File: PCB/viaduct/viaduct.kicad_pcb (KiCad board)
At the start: 2 copper layers, 76.2 x 43.2 mm, 8 parts, among them J1 n8 Bus, J2 Conn_01x03_Male, J3 Conn_01x03_Male, J4 Conn_02x12, U1 65C22S

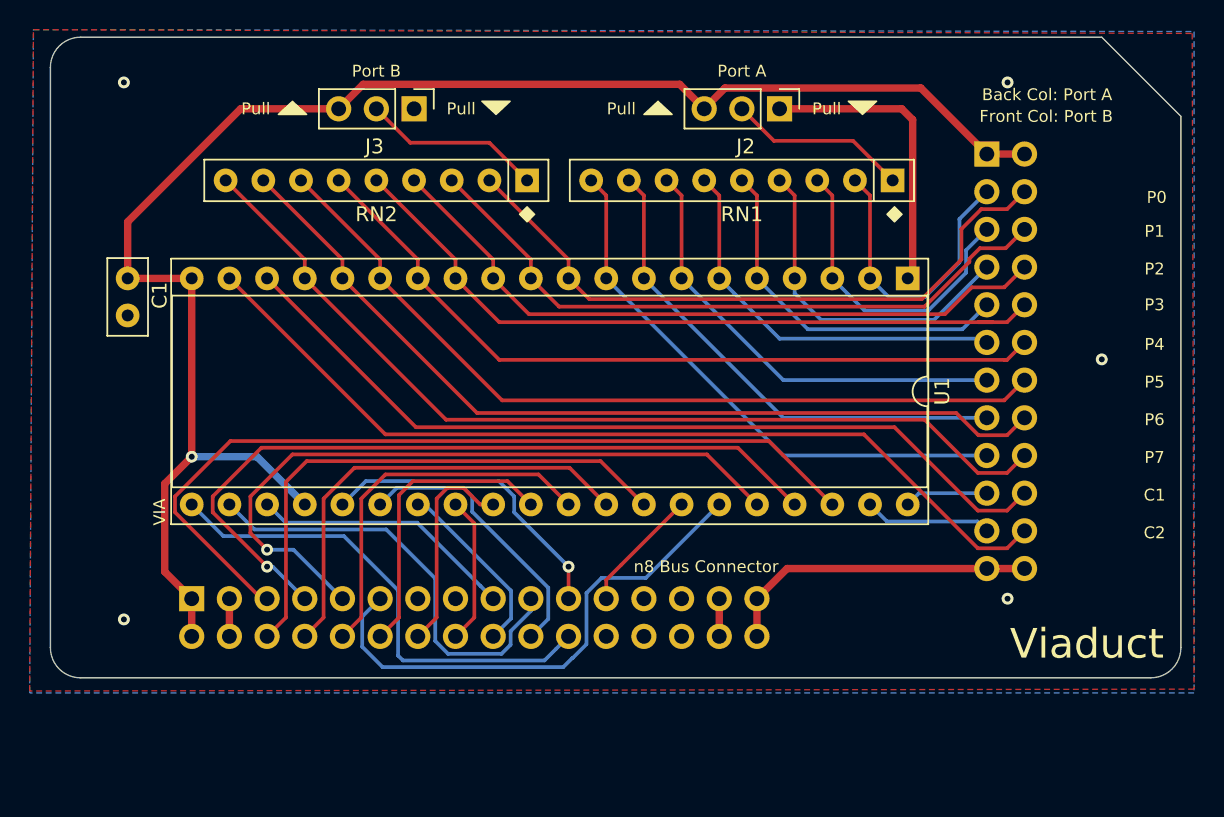
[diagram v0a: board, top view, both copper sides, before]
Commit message: New placement and parts for v2
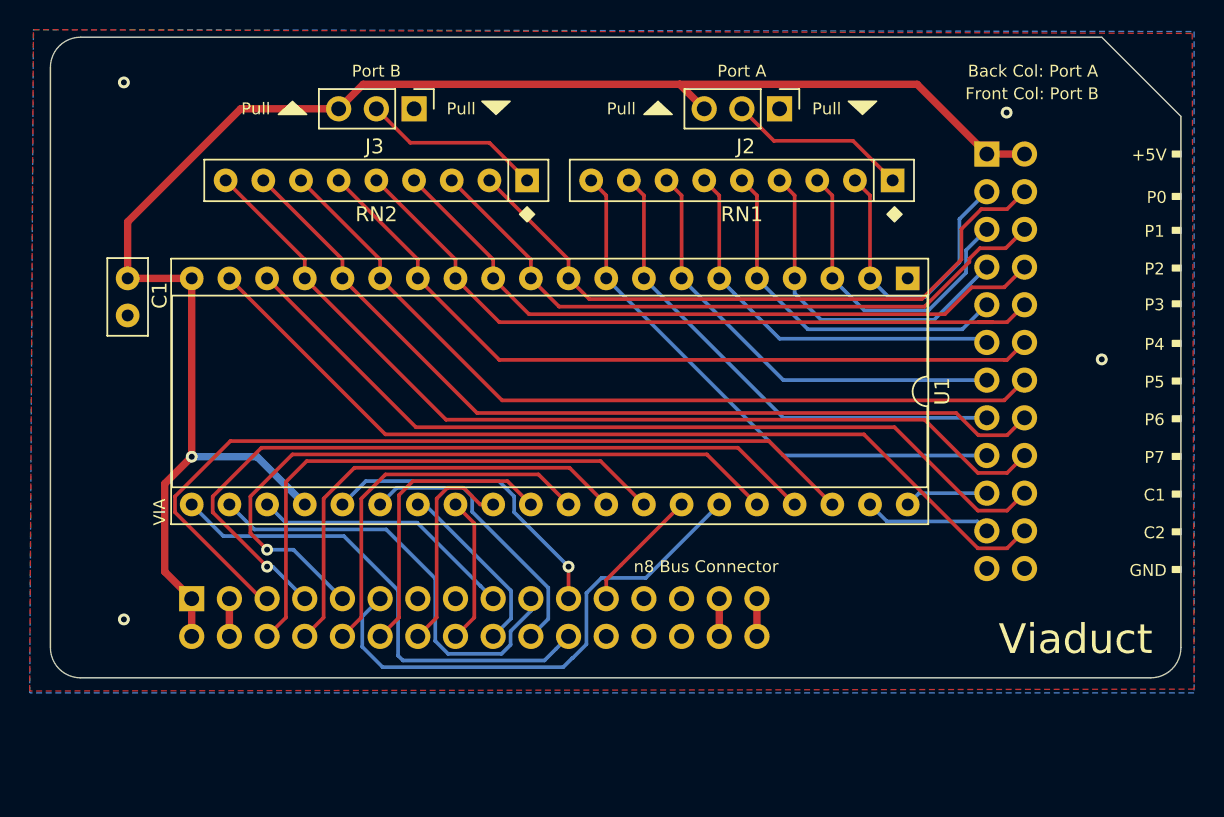
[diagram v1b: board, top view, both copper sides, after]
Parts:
- J2: value Conn_01x03_Male -> PORT_A_PULLUP_DOWN
- J3: value Conn_01x03_Male -> PORT_B_PULLUP_DOWN
- J4: value Conn_02x12 -> GPIO
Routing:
- net GND: track 44.1 -> 5.08 mm, vias 5 -> 4
- net +5V: track 110.1 -> 111.3 mm
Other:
- board text added: "+5V"
- board text added: "GND"
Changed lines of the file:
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@@
   (general
     (thickness 1.6)
-    (drawings 40)
-    (tracks 264)
+    (drawings 54)
+    (tracks 255)
     (zones 0)
     (modules 8)
@@
       (outputformat 1)
       (mirror false)
-      (drillshape 1)
+      (drillshape 0)
       (scaleselection 1)
-      (outputdirectory ""))
+      (outputdirectory "gerbers/"))
   )
   (net 0 "")
@@
       (effects (font (size 1 1) (thickness 0.15)) (justify mirror))
     )
-    (fp_text value Conn_02x12 (at -5.65 -30.71) (layer B.Fab)
+    (fp_text value GPIO (at -5.65 -30.71) (layer B.Fab)
       (effects (font (size 1 1) (thickness 0.15)) (justify mirror))
     )
@@
       (effects (font (size 1 1) (thickness 0.15)))
     )
-    (fp_text value Conn_01x03_Male (at 0 7.41 90) (layer F.Fab)
+    (fp_text value PORT_B_PULLUP_DOWN (at 0 7.41 90) (layer F.Fab)
       (effects (font (size 1 1) (thickness 0.15)))
     )
@@
       (effects (font (size 1 1) (thickness 0.15)))
     )
-    (fp_text value Conn_01x03_Male (at 0 7.41 90) (layer F.Fab)
+    (fp_text value PORT_A_PULLUP_DOWN (at 0 7.41 90) (layer F.Fab)
       (effects (font (size 1 1) (thickness 0.15)))
     )
@@
     )
   )
+  (gr_poly (pts (xy 187.579 128.27) (xy 187.0075 128.27) (xy 187.0075 127.889) (xy 187.579 127.889)) (layer F.SilkS) (width 0.1))
+  (gr_poly (pts (xy 187.579 125.73) (xy 187.0075 125.73) (xy 187.0075 125.349) (xy 187.579 125.349)) (layer F.SilkS) (width 0.1))
+  (gr_poly (pts (xy 187.579 123.19) (xy 187.0075 123.19) (xy 187.0075 122.809) (xy 187.579 122.809)) (layer F.SilkS) (width 0.1))
+  (gr_poly (pts (xy 187.579 120.65) (xy 187.0075 120.65) (xy 187.0075 120.269) (xy 187.579 120.269)) (layer F.SilkS) (width 0.1))
+  (gr_poly (pts (xy 187.579 118.11) (xy 187.0075 118.11) (xy 187.0075 117.729) (xy 187.579 117.729)) (layer F.SilkS) (width 0.1))
+  (gr_poly (pts (xy 187.579 115.57) (xy 187.0075 115.57) (xy 187.0075 115.189) (xy 187.579 115.189)) (layer F.SilkS) (width 0.1))
+  (gr_poly (pts (xy 187.579 113.03) (xy 187.0075 113.03) (xy 187.0075 112.649) (xy 187.579 112.649)) (layer F.SilkS) (width 0.1))
+  (gr_poly (pts (xy 187.579 110.363) (xy 187.0075 110.363) (xy 187.0075 109.982) (xy 187.579 109.982)) (layer F.SilkS) (width 0.1))
+  (gr_poly (pts (xy 187.579 107.95) (xy 187.0075 107.95) (xy 187.0075 107.569) (xy 187.579 107.569)) (layer F.SilkS) (width 0.1))
+  (gr_poly (pts (xy 187.579 105.41) (xy 187.0075 105.41) (xy 187.0075 105.029) (xy 187.579 105.029)) (layer F.SilkS) (width 0.1))
+  (gr_poly (pts (xy 187.579 103.124) (xy 187.0075 103.124) (xy 187.0075 102.743) (xy 187.579 102.743)) (layer F.SilkS) (width 0.1))
+  (gr_poly (pts (xy 187.579 100.2665) (xy 187.0075 100.2665) (xy 187.0075 99.8855) (xy 187.579 99.8855)) (layer F.SilkS) (width 0.1))
+  (gr_text GND (at 186.6265 128.143) (layer F.SilkS)
+    (effects (font (size 0.8 0.8) (thickness 0.15)) (justify right))
+  )
+  (gr_text +5V (at 186.6265 100.1395) (layer F.SilkS)
+    (effects (font (size 0.8 0.8) (thickness 0.15)) (justify right))
+  )
   (dimension 43.18 (width 0.15) (layer Dwgs.User)
-    (gr_text "43.180 mm" (at 190.911 113.792 270) (layer Dwgs.User)
-      (effects (font (size 1 1) (thickness 0.15)))
-    )
-    (feature1 (pts (xy 181.229 135.382) (xy 190.197421 135.382)))
-    (feature2 (pts (xy 181.229 92.202) (xy 190.197421 92.202)))
-    (crossbar (pts (xy 189.611 92.202) (xy 189.611 135.382)))
-    (arrow1a (pts (xy 189.611 135.382) (xy 189.024579 134.255496)))
-    (arrow1b (pts (xy 189.611 135.382) (xy 190.197421 134.255496)))
-    (arrow2a (pts (xy 189.611 92.202) (xy 189.024579 93.328504)))
-    (arrow2b (pts (xy 189.611 92.202) (xy 190.197421 93.328504)))
+    (gr_text "43.180 mm" (at 190.9745 113.792 270) (layer Dwgs.User)
+      (effects (font (size 1 1) (thickness 0.15)))
+    )
+    (feature1 (pts (xy 181.2925 135.382) (xy 190.260921 135.382)))
+    (feature2 (pts (xy 181.2925 92.202) (xy 190.260921 92.202)))
+    (crossbar (pts (xy 189.6745 92.202) (xy 189.6745 135.382)))
+    (arrow1a (pts (xy 189.6745 135.382) (xy 189.088079 134.255496)))
+    (arrow1b (pts (xy 189.6745 135.382) (xy 190.260921 134.255496)))
+    (arrow2a (pts (xy 189.6745 92.202) (xy 189.088079 93.328504)))
+    (arrow2b (pts (xy 189.6745 92.202) (xy 190.260921 93.328504)))
   )
   (dimension 5.334 (width 0.15) (layer Dwgs.User)
@@
     (arrow2b (pts (xy 187.579 91.567) (xy 186.452496 92.153421)))
   )
-  (gr_text "by Nate Rivard\nhttps://github.com/nrivard/lmaos\nVersion 1\nMar 2021" (at 185.674 131.572) (layer B.SilkS)
+  (gr_text "by Nate Rivard\nhttps://github.com/nrivard/lmaos\nVersion 1\nMar 2021" (at 185.674 132.1435) (layer B.SilkS)
     (effects (font (size 0.8 0.8) (thickness 0.15)) (justify left mirror))
   )
@@
     (effects (font (size 0.8 0.8) (thickness 0.15)))
   )
-  (gr_text Viaduct (at 186.436 133.096) (layer F.SilkS)
+  (gr_text Viaduct (at 185.674 132.7785) (layer F.SilkS)
     (effects (font (size 2 2) (thickness 0.3)) (justify right))
   )
@@
   (gr_arc (start 185.547 133.35) (end 185.547 135.382) (angle -90) (layer Edge.Cuts) (width 0.05))
   (gr_line (start 187.579 97.536) (end 182.245 92.202) (layer Edge.Cuts) (width 0.05))
-  (gr_text "Front Col: Port B" (at 178.4985 97.536) (layer F.SilkS)
-    (effects (font (size 0.8 0.8) (thickness 0.15)))
-  )
-  (gr_text "Back Col: Port A" (at 178.562 96.0755) (layer F.SilkS)
+  (gr_text "Front Col: Port B" (at 177.546 96.012) (layer F.SilkS)
+    (effects (font (size 0.8 0.8) (thickness 0.15)))
+  )
+  (gr_text "Back Col: Port A" (at 177.6095 94.488) (layer F.SilkS)
     (effects (font (size 0.8 0.8) (thickness 0.15)))
   )
@@
   (gr_line (start 185.547 135.382) (end 113.411 135.382) (layer Edge.Cuts) (width 0.1))
   (segment (start 159.004 132.588) (end 159.004 130.048) (width 0.5) (layer F.Cu) (net 7))
-  (via (at 175.895 95.25) (size 0.8) (drill 0.4) (layers F.Cu B.Cu) (net 7))
-  (via (at 175.895 130.048) (size 0.8) (drill 0.4) (layers F.Cu B.Cu) (net 7))
+  (via (at 175.8315 97.282) (size 0.8) (drill 0.4) (layers F.Cu B.Cu) (net 7))
   (via (at 116.332 95.25) (size 0.8) (drill 0.4) (layers F.Cu B.Cu) (net 7))
   (via (at 116.332 131.445) (size 0.8) (drill 0.4) (layers F.Cu B.Cu) (net 7))
   (via (at 182.245 113.919) (size 0.8) (drill 0.4) (layers F.Cu B.Cu) (net 7))
   (segment (start 123.444 132.588) (end 123.444 130.048) (width 0.5) (layer F.Cu) (net 7))
-  (segment (start 177.038 128.016) (end 174.498 128.016) (width 0.5) (layer F.Cu) (net 7))
-  (segment (start 161.036 128.016) (end 159.004 130.048) (width 0.5) (layer F.Cu) (net 7))
-  (segment (start 174.498 128.016) (end 161.036 128.016) (width 0.5) (layer F.Cu) (net 7))
-  (segment (start 169.498001 108.123999) (end 169.164 108.458) (width 0.5) (layer F.Cu) (net 7))
-  (segment (start 168.759998 97.028) (end 169.498001 97.766003) (width 0.5) (layer F.Cu) (net 7))
-  (segment (start 169.498001 97.766003) (end 169.498001 108.123999) (width 0.5) (layer F.Cu) (net 7))
-  (segment (start 160.528 97.028) (end 168.759998 97.028) (width 0.5) (layer F.Cu) (net 7))
   (segment (start 120.904 132.588) (end 120.904 130.048) (width 0.5) (layer F.Cu) (net 8))
   (segment (start 153.797 95.377) (end 155.448 97.028) (width 0.5) (layer F.Cu) (net 8))
@@
   (segment (start 124.206 97.028) (end 130.81 97.028) (width 0.5) (layer F.Cu) (net 8))
   (segment (start 120.904 108.458) (end 116.586 108.458) (width 0.5) (layer F.Cu) (net 8))
-  (segment (start 177.038 100.076) (end 174.498 100.076) (width 0.5) (layer F.Cu) (net 8))
-  (segment (start 170.049999 95.627999) (end 156.848001 95.627999) (width 0.5) (layer F.Cu) (net 8))
-  (segment (start 156.848001 95.627999) (end 155.448 97.028) (width 0.5) (layer F.Cu) (net 8))
-  (segment (start 174.498 100.076) (end 170.049999 95.627999) (width 0.5) (layer F.Cu) (net 8))
+  (segment (start 169.799 95.377) (end 174.498 100.076) (width 0.5) (layer F.Cu) (net 8))
+  (segment (start 153.797 95.377) (end 169.799 95.377) (width 0.5) (layer F.Cu) (net 8))
+  (segment (start 174.498 100.076) (end 177.038 100.076) (width 0.5) (layer F.Cu) (net 8))
   (segment (start 153.924 123.698) (end 149.86 127.762) (width 0.25) (layer F.Cu) (net 9))
   (segment (start 148.844 128.778) (end 148.844 130.048) (width 0.25) (layer F.Cu) (net 9))

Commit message: release candidate for v2
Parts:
- J1: value n8 Bus -> n8 Bus Connector; moved to F.Cu
- moved J1 37.1 mm to (158.1, 130.1)
- renumbered J4 to J2, J2 to J3, J3 to J4
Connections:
- J1 pad 1: +5V -> GND
- J1 pad 10: /D2 -> ~RES
- J1 pad 11: /RS3 -> ~IRQ
- J1 pad 12: /D3 -> CLK
- J1 pad 13: Net-(J1-Pad13) -> /D7
- J1 pad 14: /D4 -> R~W
- J1 pad 15: Net-(J1-Pad15) -> /D6
- J1 pad 16: /D5 -> ~CS
- J1 pad 17: ~CS -> /D5
- J1 pad 18: /D6 -> Net-(J1-Pad18)
- J1 pad 19: R~W -> /D4
- J1 pad 2: +5V -> GND
- J1 pad 20: /D7 -> Net-(J1-Pad20)
- J1 pad 21: CLK -> /D3
- J1 pad 22: ~IRQ -> /RS3
- J1 pad 23: ~RES -> /D2
- J1 pad 24: Net-(J1-Pad24) -> /RS2
- J1 pad 25: Net-(J1-Pad25) -> /D1
- J1 pad 26: Net-(J1-Pad26) -> /RS1
- J1 pad 27: Net-(J1-Pad27) -> /D0
- J1 pad 28: Net-(J1-Pad28) -> /RS0
- J1 pad 29: Net-(J1-Pad29) -> GND
- J1 pad 3: GND -> +5V
- J1 pad 30: Net-(J1-Pad29) -> GND
- J1 pad 31: GND -> +5V
- J1 pad 32: GND -> +5V
- J1 pad 4: GND -> +5V
- J1 pad 5: /RS0 -> Net-(J1-Pad5)
- J1 pad 6: /D0 -> Net-(J1-Pad6)
- J1 pad 7: /RS1 -> Net-(J1-Pad7)
- J1 pad 8: /D1 -> Net-(J1-Pad8)
- J1 pad 9: /RS2 -> Net-(J1-Pad9)
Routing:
- net +5V: track 111.3 -> 145.8 mm, vias 1 -> 0
- net R~W: track 29.5 -> 56.6 mm
- net /RS0: track 58.2 -> 45.1 mm
- net /RS2: track 47.2 -> 35.0 mm, vias 1 -> 0
- net /RS1: track 51.9 -> 41.4 mm, vias 1 -> 0
- net /D7: track 19.0 -> 12.2 mm, vias 0 -> 1
- net /RS3: track 34.9 -> 28.4 mm
- net GND: track 5.08 -> 0.00 mm
- net /D4: track 14.4 -> 9.66 mm
- net /D0: track 36.9 -> 32.4 mm
- net /D3: track 20.0 -> 16.0 mm
- net /D1: track 30.7 -> 26.9 mm
- net /D2: track 25.3 -> 21.5 mm
- net ~RES: track 8.45 -> 11.6 mm
- net /D5: track 9.94 -> 6.77 mm
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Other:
- board text added: "JLCJLCJLCJLC"
- board text added: "by Nate Rivard https://github.com/nrivard/lmaos Version 2 Dec 2021"
- board text removed: "by Nate Rivard https://github.com/nrivard/lmaos Version 1 Mar 2021"
